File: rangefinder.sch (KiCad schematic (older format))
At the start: 5 parts, among them U8 VL53L0X

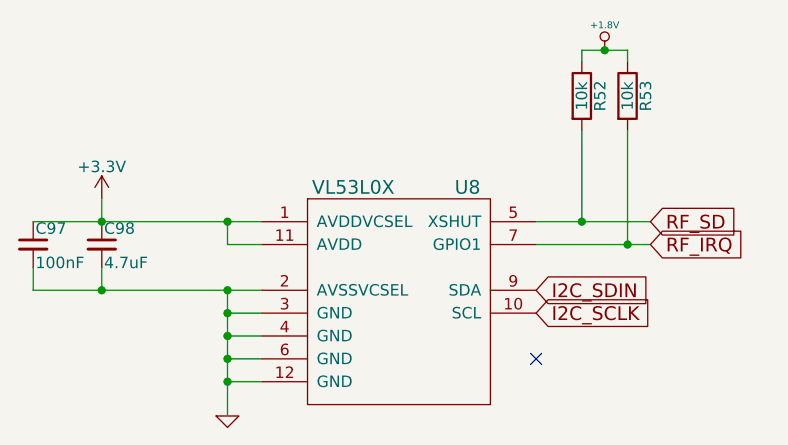
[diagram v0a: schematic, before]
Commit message: reannotated, created some footprints
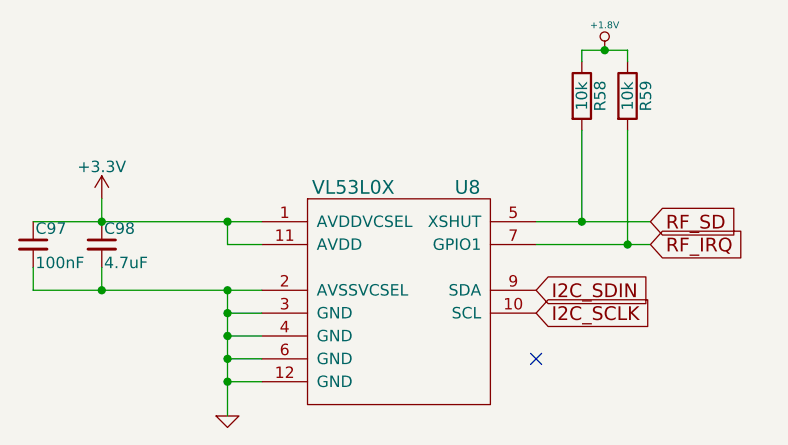
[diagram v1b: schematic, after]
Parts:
- renumbered R52 to R58, R53 to R59
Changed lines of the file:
@@
 NoConn ~ 5900 3900
 $Comp
-L GND-RESCUE-DFTBoard #PWR125
+L GND-RESCUE-DFTBoard #PWR0126
 U 1 1 58598433
 P 4550 4150
-F 0 "#PWR125" H 4550 4150 30  0001 C CNN
+F 0 "#PWR0126" H 4550 4150 30  0001 C CNN
 F 1 "GND" H 4550 4080 30  0001 C CNN
 F 2 "" H 4550 4150 60  0001 C CNN
@@
 RF_SD
 $Comp
-L R R52
+L R R58
 U 1 1 58598665
 P 6100 2750
-F 0 "R52" V 6180 2750 50  0000 C CNN
+F 0 "R58" V 6180 2750 50  0000 C CNN
 F 1 "10k" V 6100 2750 50  0000 C CNN
 F 2 "Resistors_SMD:R_1206" V 6030 2750 50  0001 C CNN
@@
 $EndComp
 $Comp
-L R R53
+L R R59
 U 1 1 585986E0
 P 6300 2750
-F 0 "R53" V 6380 2750 50  0000 C CNN
+F 0 "R59" V 6380 2750 50  0000 C CNN
 F 1 "10k" V 6300 2750 50  0000 C CNN
 F 2 "Resistors_SMD:R_1206" V 6230 2750 50  0001 C CNN
@@
 	5900 3300 6400 3300
 $Comp
-L +1.8V #PWR126
+L +1.8V #PWR0127
 U 1 1 585987BD
 P 6200 2550
-F 0 "#PWR126" H 6200 2690 20  0001 C CNN
+F 0 "#PWR0127" H 6200 2690 20  0001 C CNN
 F 1 "+1.8V" H 6200 2660 30  0000 C CNN
 F 2 "" H 6200 2550 60  0001 C CNN
@@
 RF_IRQ
 $Comp
-L +3.3V #PWR124
+L +3.3V #PWR0128
 U 1 1 587438B2
 P 4000 3200
-F 0 "#PWR124" H 4000 3050 50  0001 C CNN
+F 0 "#PWR0128" H 4000 3050 50  0001 C CNN
 F 1 "+3.3V" H 4000 3340 50  0000 C CNN
 F 2 "" H 4000 3200 50  0000 C CNN

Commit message: finished a quarter to a third of non-priority connections
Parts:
- R58, R59: footprint Resistors_SMD:R_1206 -> Resistors_SMD:R_0402
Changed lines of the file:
@@
 F 0 "R58" V 6180 2750 50  0000 C CNN
 F 1 "10k" V 6100 2750 50  0000 C CNN
-F 2 "Resistors_SMD:R_1206" V 6030 2750 50  0001 C CNN
+F 2 "Resistors_SMD:R_0402" V 6030 2750 50  0001 C CNN
 F 3 "" H 6100 2750 50  0000 C CNN
 	1    6100 2750
@@
 F 0 "R59" V 6380 2750 50  0000 C CNN
 F 1 "10k" V 6300 2750 50  0000 C CNN
-F 2 "Resistors_SMD:R_1206" V 6230 2750 50  0001 C CNN
+F 2 "Resistors_SMD:R_0402" V 6230 2750 50  0001 C CNN
 F 3 "" H 6300 2750 50  0000 C CNN
 	1    6300 2750

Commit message: finished most non-priority connections and placed power/gnd planes
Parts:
- U8: footprint DFTcustom:LGA12 -> DFTcustom:Optical_LGA12
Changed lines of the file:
@@
 LIBS:au-y1008-2
 LIBS:hdmi_conn
+LIBS:wayne_and_layne_kicad_symbols
 EELAYER 25 0
 EELAYER END
@@
 F 0 "U8" H 5600 4250 60  0000 C CNN
 F 1 "VL53L0X" H 5100 4250 60  0000 C CNN
-F 2 "DFTcustom:LGA12" H 5350 3650 60  0001 C CNN
+F 2 "DFTcustom:Optical_LGA12" H 5350 3650 60  0001 C CNN
 F 3 "" H 5350 3650 60  0000 C CNN
 	1    5300 3700
@@
 NoConn ~ 5900 3900
 $Comp
-L GND-RESCUE-DFTBoard #PWR0126
+L GND-RESCUE-DFTBoard #PWR0135
 U 1 1 58598433
 P 4550 4150
-F 0 "#PWR0126" H 4550 4150 30  0001 C CNN
+F 0 "#PWR0135" H 4550 4150 30  0001 C CNN
 F 1 "GND" H 4550 4080 30  0001 C CNN
 F 2 "" H 4550 4150 60  0001 C CNN
@@
 	5900 3300 6400 3300
 $Comp
-L +1.8V #PWR0127
+L +1.8V #PWR0136
 U 1 1 585987BD
 P 6200 2550
-F 0 "#PWR0127" H 6200 2690 20  0001 C CNN
+F 0 "#PWR0136" H 6200 2690 20  0001 C CNN
 F 1 "+1.8V" H 6200 2660 30  0000 C CNN
 F 2 "" H 6200 2550 60  0001 C CNN
@@
 RF_IRQ
 $Comp
-L +3.3V #PWR0128
+L +3.3V #PWR0137
 U 1 1 587438B2
 P 4000 3200
-F 0 "#PWR0128" H 4000 3050 50  0001 C CNN
+F 0 "#PWR0137" H 4000 3050 50  0001 C CNN
 F 1 "+3.3V" H 4000 3340 50  0000 C CNN
 F 2 "" H 4000 3200 50  0000 C CNN
